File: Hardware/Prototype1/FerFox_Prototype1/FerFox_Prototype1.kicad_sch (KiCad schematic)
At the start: 38 parts, among them J1 Conn_01x08_Pin, J2 Conn_01x06_Pin, U1 STM32F401CCUx, U2 LY68L6400, Y1 25MHz, Y2 32768 Hz

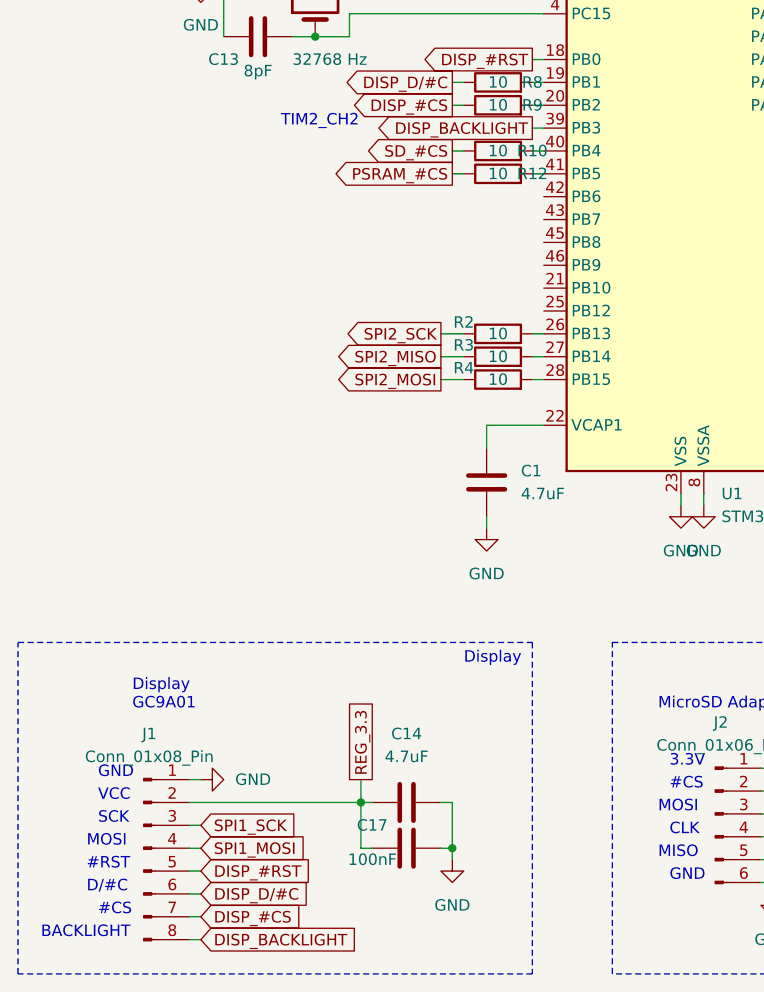
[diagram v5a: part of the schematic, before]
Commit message: Bigger noise-cancelling resistors
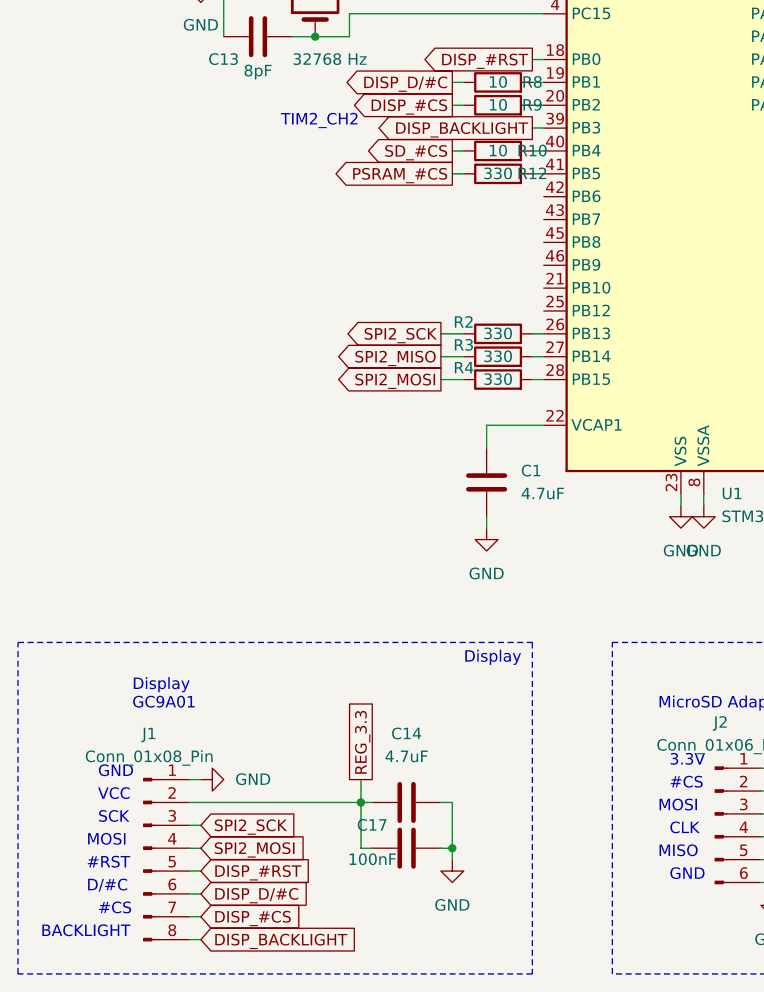
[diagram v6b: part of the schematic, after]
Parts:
- R12, R2, R3, R4: value 10 -> 330
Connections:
- net SPI1_MOSI: no longer J1.4 (Pin_4)
- net SPI1_SCK: no longer J1.3 (Pin_3)
- net SPI2_MOSI: now also J1.4 (Pin_4)
- net SPI2_SCK: now also J1.3 (Pin_3)
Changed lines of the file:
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@@
     )
   )
-  (global_label "SPI1_MOSI" (shape input) (at 167.64 181.61 0) (fields_autoplaced)
+  (global_label "SPI2_MOSI" (shape input) (at 167.64 181.61 0) (fields_autoplaced)
     (effects (font (size 1.27 1.27)) (justify left))
     (property "Intersheetrefs" "${INTERSHEET_REFS}" (at 180.4828 181.61 0)
@@
     )
   )
-  (global_label "SPI1_SCK" (shape input) (at 167.64 179.07 0) (fields_autoplaced)
+  (global_label "SPI2_SCK" (shape input) (at 167.64 179.07 0) (fields_autoplaced)
     (effects (font (size 1.27 1.27)) (justify left))
     (property "Intersheetrefs" "${INTERSHEET_REFS}" (at 179.6361 179.07 0)
@@
       (effects (font (size 1.27 1.27)))
     )
-    (property "Value" "10" (at 200.66 129.54 90)
+    (property "Value" "330" (at 200.66 129.54 90)
       (effects (font (size 1.27 1.27)))
     )
@@
       (effects (font (size 1.27 1.27)))
     )
-    (property "Value" "10" (at 200.66 106.68 90)
+    (property "Value" "330" (at 200.66 106.68 90)
       (effects (font (size 1.27 1.27)))
     )
@@
       (effects (font (size 1.27 1.27)))
     )
-    (property "Value" "10" (at 200.66 124.46 90)
+    (property "Value" "330" (at 200.66 124.46 90)
       (effects (font (size 1.27 1.27)))
     )
@@
       (effects (font (size 1.27 1.27)))
     )
-    (property "Value" "10" (at 200.66 127 90)
-      (effects (font (size 1.27 1.27)))
-    )
+    (property "Value" "330" (at 200.66 127 90)
+      (effects (font (size 1.27 1.27)))
+    )
